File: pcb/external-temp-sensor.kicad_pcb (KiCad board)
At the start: 2 copper layers, 29.5 x 38.1 mm, 13 parts, among them P1 TEMP, P2 SERIAL, P3 PWR, SW1 RESET, SW2 FLASH, U1 ESP-12F, U2 OKI-78SR

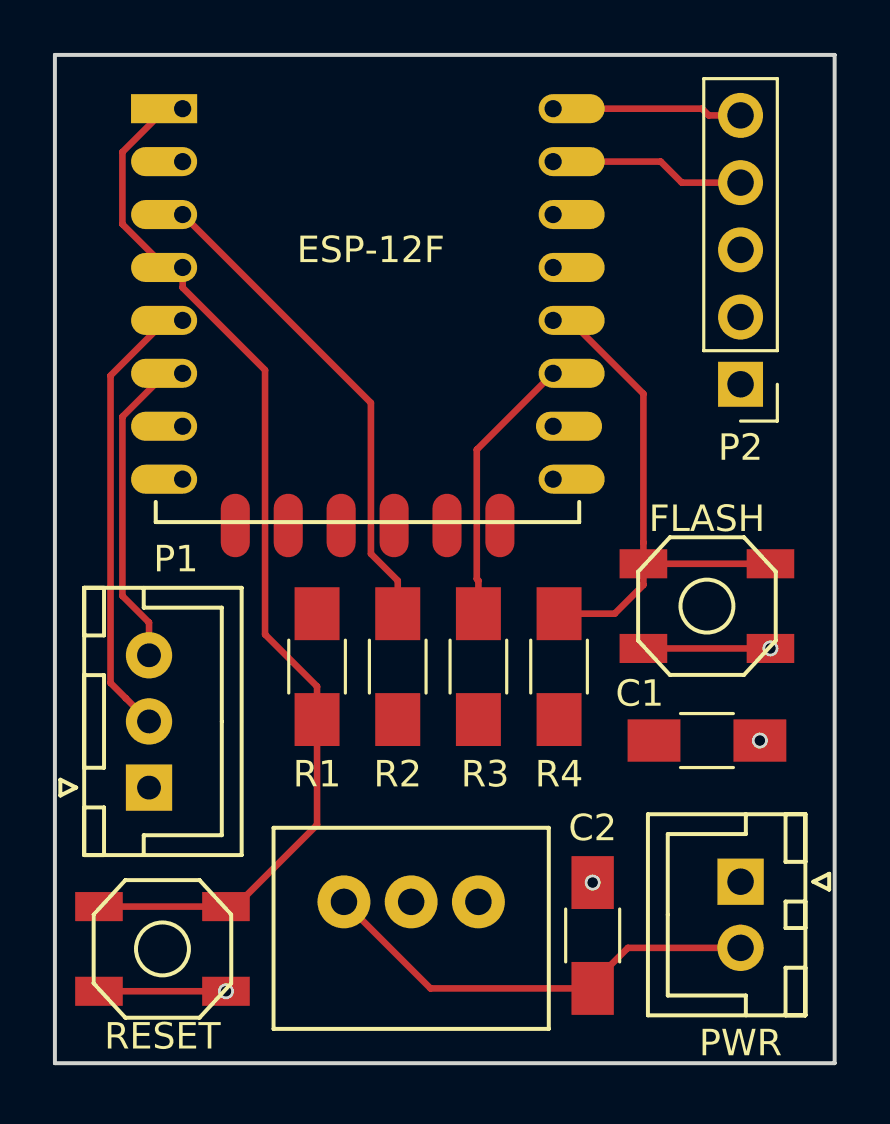
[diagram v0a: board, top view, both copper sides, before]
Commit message: Add pull-up resistor
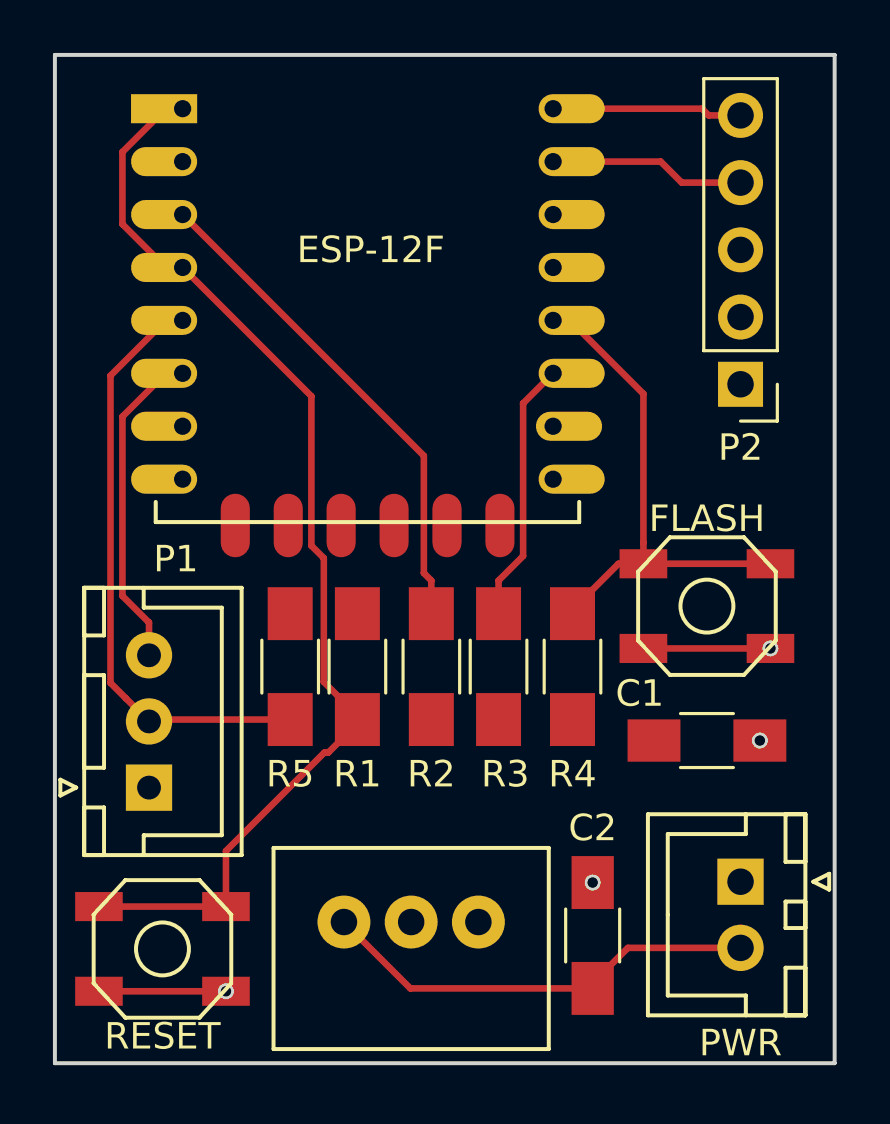
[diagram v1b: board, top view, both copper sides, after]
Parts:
- added R5: 4.7K, Resistors_SMD:R_1206_HandSoldering, F.Cu at (154.2, 103.9)
- moved R1 1.52 mm to (156.7, 103.9)
- moved R2 1.27 mm to (159.5, 103.9)
- moved R3 0.76 mm to (162.1, 103.9)
- moved U2 0.76 mm to (158.8, 113.5)
- moved R4 0.51 mm to (164.8, 103.9)
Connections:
- net /DS18S20_DQ renamed /DS18B20_DQ
- net /DS18S20_PWR renamed /DS18B20_PWR
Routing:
- net /DS18B20_DQ: track 17.3 -> 22.6 mm
- net /RESET: track 41.3 -> 42.8 mm
- net /FLASH: track 20.2 -> 19.3 mm
- net /CH_EN: track 18.4 -> 19.0 mm
